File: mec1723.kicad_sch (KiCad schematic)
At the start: 62 parts, among them SW3001 SW_B3U-1000P_SMD, SW3002 SW_B3U-1000P_SMD, SW3003 SW_B3U-1000P_SMD, U3001 MEC1723N-B0-I/SZ, Y3001 Resonator_32.768kHz_ECX-31B

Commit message: [#103224] Add strapping pins, check for signals needed to boot, add breakout connectors, add testpoints
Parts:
- added J3001, J3002, J3003, J3004, J3005, J3006, J3007, J3008, J3009: PinHeader_2x5_P1.27mm_SMD, antmicro-footprints:PinHeader_2x5_P1.27mm_SMD, symbol Antmicro Symbols:PinHeader_2x5_P1.27mm_SMD
- added R3033, R3034, R3035, R3036: R_10k_0402, antmicro-footprints:R_0402_1005Metric, symbol Antmicro Symbols:R_10k_0402
- added TP3008, TP3009, TP3010, TP3011, TP3012: TP_1mm_SMD, antmicro-footprints:TP_SMD_1mm, symbol antmicroTestPoints:TP_1mm_SMD
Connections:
- net +1V8: now also J3004.3, TP3008.1
- net +3V3: now also TP3001.1, J3003.7, J3004.1, R3033.2, R3035.2, TP3009.1, TP3011.1
- net 7SEG_H.A: now also U3001.N10 (GPIO152/KSO14/GPTP_OUT3/I2C07_SDA_ALT)
- net 7SEG_H.B: now also U3001.B9 (GPIO254)
- net 7SEG_H.C: now also U3001.A13 (GPIO156/LED0)
- net 7SEG_H.D: now also U3001.B13 (GPIO157/LED1)
- net 7SEG_H.DP: now also U3001.A9 (GPIO165/32KHZ_IN/CTOUT0)
- net 7SEG_H.E: now also U3001.C12 (GPIO153/LED2)
- net 7SEG_H.F: now also U3001.E13 (GPIO035/PWM8/CTOUT1/ICT15/LED3)
- net 7SEG_H.G: now also U3001.C13 (GPIO175/CMP_VOUT1/PWM8_ALT)
- net 7SEG_H.~{OE1}: now also U3001.C1 (GPIO221/32KHz_OUT/GPTP_IN3/CMP_VIN1/SYS-_SHDN_FW#)
- net 7SEG_H.~{OE2}: now also U3001.B8 (GPIO241/CMP_VOUT0/PWM0_ALT)
- net 7SEG_L.A: now also U3001.L7 (GPIO020/KSI1)
- net 7SEG_L.B: now also U3001.N9 (GPIO021/KSI2)
- net 7SEG_L.C: now also U3001.J9 (GPIO030/KSI5/I2C10_SDA/TIN3)
- net 7SEG_L.D: now also U3001.M11 (GPIO031/KSI6/GPTP_OUT1)
- net 7SEG_L.DP: now also U3001.J5 (GPIO064/SLP_S0#)
- net 7SEG_L.E: now also U3001.M10 (GPIO040/GPTP_OUT2/KSO00)
- net 7SEG_L.F: now also U3001.J12 (GPIO042/PECI_DAT/SB-TSI_DAT)
- net 7SEG_L.G: now also U3001.J13 (GPIO043/SB-TSI_CLK)
- net 7SEG_L.~{OE1}: now also U3001.G13 (GPIO240)
- net 7SEG_L.~{OE2}: now also U3001.L9 (GPIO151/ICT4/KSO15)
- net CMP_STRAP: now also R3033.1, R3034.2
- net DC_SCM_P3V0: now also TP3010.1
- net GND: now also R3032.1, J3003.9, J3004.5, J3004.7, J3004.9, R3034.1, R3036.1, TP3012.1
- net PWRGD_S0iX: now also J3003.5
- net UART_BSTRAP: now also R3035.1, R3036.2
- net GPIO143: now reaches R3013.1, U3001.A7 (GPIO143/I2C04_SDA/UART0_CTS#/SPI1_MISO/UART0_DTR#_ALT)
- net GPIO143: now also J3001.8
- net GPIO154: now reaches R3009.1, U3001.A12 (GPIO154/I2C02_SDA/CPU_C10)
- net GPIO154: now also J3008.10
- net GPIO131: now reaches R3008.1, U3001.N7 (GPIO131/I2C01_SCL/SLV_SPI_CS#/TOUT0)
- net GPIO131: now also J3008.8
- net GPIO004: now reaches R3022.1, U3001.C6 (GPIO004/I2C00_SCL/SPI0_MOSI)
- net GPIO004: now also J3006.6
- net GPIO010: now reaches R3012.1, U3001.C10 (GPIO010/I2C03_SCL/PS2_DAT0B)
- net GPIO010: now also J3001.6
- net GPIO003: now reaches R3021.1, U3001.F5 (GPIO003/I2C00_SDA/SPI0_CS0#)
- net GPIO003: now also J3006.4
- net GPIO242: now reaches U3001.A10 (GPIO242/VCC_PWRGD_ALT)
- net GPIO242: now also J3002.1
- net GPIO224: now reaches U3001.A11 (GPIO244/UART_CLK_ALT/PWROK_ALT)
- net GPIO224: now also J3005.5
- net GPIO062: now reaches U3001.A2 (GPIO062/I2C11_SCL(RESET#))
- net GPIO062: now also J3005.1
- net GPIO246: now reaches U3001.B10 (GPIO246/PWRGD_S0iX_ALT2/CTOUT1_ALT)
- net GPIO246: now also J3005.7
- net GPIO000: now reaches U3001.B3 (SYSPWR_PRES&VCI_IN3#/GPIO000/I2C11_SDA)
- net GPIO106: now reaches U3001.E3 (GPIO106/PWROK/CMP_VREF1)
- net GPIO106: now also J3005.3
- net GPIO067: now reaches U3001.L2 (GPIO067/VREF2_ADC)
- net GPIO067: now also J3004.10
- net GPIO222: now reaches U3001.L5 (GPIO222/PROCHOT_IN#_ALT)
- net GPIO222: now also J3002.3
- net GPIO002: now reaches U3001.M8 (GPIO002/PWM5/SHD_CS1#)
- net GPIO002: now also J3006.3
- net GPIO144: now reaches R3014.1, U3001.E7 (GPIO144/I2C04_SCL/UART0_RTS#/SPI1_CS#/UART0_RI#_ALT)
- net GPIO144: now also J3001.10
- net GPIO012: now reaches R3019.1, U3001.N6 (GPIO012/I2C07_SDA/SLV_SPI_IO2/TOUT3)
- net GPIO012: now also J3002.10
- net GPIO142: now reaches R3016.1, U3001.F7 (GPIO142/I2C05_SCL/SPI1_MOSI/UART0_DSR#_ALT)
- net GPIO142: now also J3002.4
- net GPIO112: now reaches U3001.K13 (GPIO112/KSO05(DSW_PWRGD))
- net GPIO112: now also J3008.3; no longer TP3001.1
- net GPIO130: now reaches R3007.1, U3001.N8 (GPIO130/I2C01_SDA/SLV_SPI_IO0/TOUT1)
- net GPIO130: now also J3008.6
- net BGP01: now reaches U3001.A4 (BGPO1/GPIO101)
- net BGP01: now also J3003.8
- net BGP00: now reaches U3001.A5 (BGPO0)
- net BGP00: now also J3003.6
- net ~{VCI_IN1}: now reaches U3001.A6 (VCI_IN1#/GPIO162)
- net ~{VCI_IN1}: now also J3003.2
- net GPIO051: now reaches U3001.B1 (GPIO051/ICT1_TACH1/GTACH1)
- net GPIO051: now also J3001.1
- net GPIO245: now reaches U3001.B11 (GPIO245/GPSPI_I00)
- net GPIO245: now also J3009.5, J3009.6
- net GPIO033: now reaches U3001.B2 (GPIO033/TACH3/RC_ID0)
- net GPIO033: now also J3001.7
- net BGP02: now reaches U3001.B5 (BGPO2/GPIO102)
- net BGP02: now also J3003.10
- net GPIO124: now reaches U3001.C11 (GPIO124/PVT_CS#/KS011/ICT12/GPTP_OUT6)
- net GPIO124: now also J3007.9
- net GPIO024: now reaches U3001.C2 (GPIO024/GPSPI_CS#/GTPP_IN6/I2C07_SCL_ALT)
- net GPIO024: now also J3009.3, J3009.4
- net GPIO023: now reaches U3001.C3 (GPIO023/GPSPI_CLK/GPTP_IN7)
- net GPIO023: now also J3009.1, J3009.2
- net ~{VCI_IN2}: now reaches U3001.C4 (VCI_IN2#/GPIO161)
- net ~{VCI_IN2}: now also J3003.4
- net VCI_OUT2: now reaches U3001.C5 (VCI_OUT2)
- net VCI_OUT2: now also J3003.3
- net GPIO243: now reaches U3001.C8 (GPIO243/GPSPI_I01)
- net GPIO243: now also J3009.7, J3009.8
- net GPIO125: now reaches U3001.D11 (GPIO125/PVT_CLK/KS012/GPTP_OUT5)
- net GPIO125: now also J3008.1
- net GPIO122: now reaches U3001.E11 (GPIO122/PVT_I01/KS009)
- net GPIO122: now also J3007.5
- net GPIO123: now reaches U3001.E12 (GPIO123/PVT_I02/KS010)
- net GPIO123: now also J3007.7
- net GPIO022: now reaches U3001.E2 (GPIO022/GPSPI_IO3/GPTP_IN4/32kHz_OUT_ALT)
- net GPIO022: now also J3009.10, J3009.9
- net GPIO046: now reaches U3001.E9 (GPIO046/KS002/ICT11/BCM1_DAT)
- net GPIO046: now also J3007.1
- net VCI_OVRD_IN: now reaches U3001.F1 (VCI_OVRD_IN)
- net VCI_OVRD_IN: now also J3003.1
- net GPIO121: now reaches U3001.F12 (GPIO121/PVT_I00/KS008)
- net GPIO121: now also J3007.3
- net GPIO047: now reaches U3001.F13 (GPIO047/KS003/PWM3_ALT/ICT13/BCM1_CLK)
- net GPIO047: now also J3005.9
- net GPIO050: now reaches U3001.F3 (GPIO050/ICT0_TACH0/GTACH0)
- net GPIO050: now also J3001.3
- net GPIO204: now reaches U3001.H2 (GPIO204/ADC04)
- net GPIO204: now also J3004.4
- net GPIO200: now reaches U3001.H3 (GPIO200/ADC00/TRACEDATA0)
- net GPIO200: now also J3006.5
- net GPIO114: now reaches U3001.H9 (GPIO114/PS2_CLK0A/nEC_SCI)
- net GPIO114: now also U3001.N12 (GPIO115/PS2_DAT0A), J3008.7, J3008.9
- net GPIO203: now reaches U3001.J1 (GPIO203/ADC03/TRACEDATA3)
- net GPIO203: now also J3004.2
- net GPIO113: now reaches U3001.J11 (GPIO113/KSO06/ICT9)
- net GPIO113: now also J3008.5
- net GPIO202: now reaches U3001.J2 (GPIO202/ADC02/TRACEDATA2)
- net GPIO202: now also J3006.9
- net GPIO201: now reaches U3001.J3 (GPIO201/ADC01/TRACEDATA1)
- net GPIO201: now also J3006.7
- net GPIO015: now reaches U3001.J7 (GPIO015/PWM7/ICT10)
- net GPIO015: now also J3002.9
- net GPIO205: now reaches U3001.K3 (GPIO205/ADC05)
- net GPIO205: now also J3004.6
- net GPIO206: now reaches U3001.L1 (GPIO206/ADC06)
- net GPIO206: now also J3004.8
- net GPIO054: now reaches U3001.L12 (GPIO054/PWM1/SLV_SPI_SCLK/GPWM1)
- net GPIO054: now also J3002.5
- net GPIO052: now reaches U3001.L8 (GPIO052/ICT2_TACH2)
- net GPIO052: now also J3001.5
- net GPIO053: now reaches U3001.M13 (GPIO053/PWM0/SLV_SPI_MSTR_INT/GPWM0)
- net GPIO053: now also J3001.9
- net GPIO014: now reaches U3001.M9 (GPIO014/PWM6/SLV_SPI_IO1/GPTP_IN2)
- net GPIO014: now also J3002.7
- net GPIO155: now reaches R3010.1, U3001.C9 (GPIO155/I2C02_SCL(SYSPWR_VALID))
- net GPIO155: now also J3001.2
- net GPIO007: now reaches R3011.1, U3001.B12 (GPIO007/I2C03_SDA/PS2_CLK0B)
- net GPIO007: now also J3001.4
- net GPIO013: now reaches R3020.1, U3001.M7 (GPIO013/I2C07_SCL/SLV_SPI_IO3/TOUT2)
- net GPIO013: now also J3006.1
- net GPIO141: now reaches R3015.1, U3001.B7 (GPIO141/I2C05_SDA/SPI1_CLK/UART0_DCD#_ALT)
- net GPIO141: now also J3002.2
- net GPIO255: now reaches U3001.B6 (GPIO255/UART1_RX_ALT/UART1_DSR#)
- net GPIO255: now also J3007.8
- net GPIO060: now reaches U3001.D2 (GPIO060/KBRST/TST_-CLK_OUT/UART1_DCD#/SPI0_CS1#)
- net GPIO060: now also J3007.4
- net GPIO171: now reaches U3001.G9 (GPIO171/UART1_RX/TFDP_DATA)
- net GPIO171: now also J3005.2
- net GPIO034: now reaches R3024.1, U3001.H12 (GPIO034/GPSPI_IO2/RC_ID1/SPI0_CLK)
- net GPIO034: now also J3006.10
- net GPIO036: now reaches R3023.1, U3001.H13 (GPIO036/RC_ID2/SPI0_MISO)
- net GPIO036: now also J3006.8
- net GPIO100: now reaches U3001.H7 (GPIO100/nEC_SCI_ALT/ICT6)
- net GPIO100: now also J3006.2
- net GPIO011: now reaches U3001.J6 (GPIO011/nSMI_ALT/PWM4/ICT7)
- net GPIO011: now also J3008.2
- net GPIO120: now reaches U3001.K12 (GPIO120/KSO07/UART1_DTR#)
- net GPIO120: now also J3007.6
- net GPIO140: now reaches R3018.1, U3001.L11 (GPIO140/I2C06_SCL/ICT5/KSO17)
- net GPIO140: now also J3002.8
- net GPIO107: now reaches U3001.L13 (GPIO107/nSMI/KSO04/I2C10_SCL)
- net GPIO107: now also J3008.4
- net GPIO025: now reaches U3001.M12 (GPIO025/nEMI_INT/UART_CLK/UART1_RI#/TIN0)
- net GPIO025: now also J3007.10
- net GPIO132: now reaches R3017.1, U3001.N11 (GPIO132/I2C06_SDA/KSO16)
- net GPIO132: now also J3002.6
- net ~{UART0_CTS} renamed GPIO127
- net GPIO127: now also J3005.4
- net ~{UART0_DCD} renamed GPIO17
- net GPIO17: now also J3005.6
- net ~{UART0_DSR} renamed GPIO027
- net GPIO027: now also J3005.10
- net ~{UART0_DTR} renamed GPIO026
- net GPIO026: now also J3005.8
- net ~{UART0_RI} renamed GPIO032
- net GPIO032: now also J3007.2
- no-connect marks 2 -> 0
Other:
- note added: "Boot Source Select Strap: - 1(R5010 not mounted)=Use the shared SPI pins for boot - 0(R5010 mounted)=Use the eSPI Flash Channel for boot"
- note added: "Check if needed"
- note added: "PIN BREAKOUT"
- note added: "PVT Flash"
- note removed: "ADC pins"
- note removed: "Boot Source Select Strap: 1(R5010 not mounted)=Use the shared SPI pins for boot 0(R5010 mounted)=Use the eSPI Flash Channel for boot"
- note removed: "Connect GPIO after connecting all other, most important signals"
- note removed: "Private QSPI Flash"
- moved on the sheet: C3007, C3008, C3009, C3010, C3013, C3015, C3016, C3018, R3001, R3002, R3005, R3006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

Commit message: [#103224] Add pullup resistors to VCI_IN#, add pulldown to nRSMRST, add schottky diode on VBAT
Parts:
- removed C3001: C_1u_6.3V_X6S_0402, antmicro-footprints:C_0402_1005Metric, symbol Antmicro Symbols:C_1u_6.3V_X6S_0402
- removed C3014, C3015, C3016, C3017: C_1u_10V_X7R_0603, antmicro-footprints:C_0603_1608Metric, symbol Antmicro Symbols:C_1u_10V_X7R_0603
- added C3001, C3014, C3015, C3016, C3017: C_1u_0603, antmicro-footprints:C_0603_1608Metric, symbol Antmicro Symbols:C_1u_0603
- added D3001: BAT54-02V-G3-08, antmicro-footprints:SOD-523, symbol Antmicro Symbols:BAT54-02V-G3-08
- added R3037: R_1k_0402, antmicro-footprints:R_0402_1005Metric, symbol Antmicro Symbols:R_1k_0402
- added R3038, R3039, R3040: R_100k_0402, antmicro-footprints:R_0402_1005Metric, symbol Antmicro Symbols:R_100k_0402
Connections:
- net +1V8: now also C3016.2
- net +3V3: now also C3015.2, C3017.2
- net GND: now also C3001.1, C3014.1, C3015.1, C3016.1, C3017.1, R3040.1
- net GPIO171: no longer U3001.G9 (GPIO171/UART1_RX/TFDP_DATA)
- net ~{VCI_IN1}: no longer U3001.A6 (VCI_IN1#/GPIO162)
- net ~{VCI_IN2}: no longer U3001.C4 (VCI_IN2#/GPIO161)
- net at U3001.H1 (VR_CAP): now also C3001.2
- net DC_SCM_P3V0 renamed +3V0
- net +3V0: now also C3014.2, R3037.1, R3038.2, R3039.2; no longer U3001.E5 (VBAT)
- new net: D3001.2 (A), R3037.2
- new net: D3001.1 (C), U3001.E5 (VBAT)
- new net: R3039.1, U3001.C4 (VCI_IN2#/GPIO161)
- new net: R3038.1, U3001.A6 (VCI_IN1#/GPIO162)
- new net ~{RSMRST}: R3040.2, U3001.G9 (GPIO171/UART1_RX/TFDP_DATA)
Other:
- note added: "If the Shared SPI port is used for booting, then any unused GPIO may be used for RSMRST#."
- note added: "SPI Flash used - ~{RSMRST} signal can be on any GPIO"
- note removed: "Alt fundtion: RSMRST#"
- note removed: "VTR1: VTR2: - eSPI"
- moved on the sheet: C3002, C3003, C3004, C3005, C3006, C3007, C3008, C3009, C3010, C3011, C3012, C3013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

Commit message: [#103224] Add UART1, added GND to breakout connectors, fix orientation of DC-SCM connector, delete unused notes
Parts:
- added J3010, J3011: PinHeader_2x5_P1.27mm_SMD, antmicro-footprints:PinHeader_2x5_P1.27mm_SMD, symbol Antmicro Symbols:PinHeader_2x5_P1.27mm_SMD
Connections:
- net 7SEG_H.~{OE2} is gone; now on net 7SEG_H.DP: U3001.B8 (GPIO241/CMP_VOUT0/PWM0_ALT)
- net 7SEG_L.~{OE1} is gone; now on net 7SEG_L.F: U3001.G13 (GPIO240)
- net 7SEG_L.~{OE2} is gone; now on net 7SEG_L.DP: U3001.L9 (GPIO151/ICT4/KSO15)
- net +1V8: no longer J3004.3
- net +3V3: no longer J3003.7, J3004.1
- net 7SEG_H.DP: no longer U3001.A9 (GPIO165/32KHZ_IN/CTOUT0)
- net 7SEG_L.DP: no longer U3001.J5 (GPIO064/SLP_S0#)
- net 7SEG_L.F: no longer U3001.J12 (GPIO042/PECI_DAT/SB-TSI_DAT)
- net BGP00: now also J3004.1; no longer J3003.6
- net GND: now also J3001.5, J3001.6, J3002.5, J3002.6, J3003.5, J3003.6, J3004.6, J3005.5, J3005.6, J3006.5, J3006.6, J3007.5, J3007.6, J3008.5, J3008.6, J3009.5, J3009.6, J3010.5, J3010.6, J3011.6; no longer J3003.9, J3004.7, J3004.9
- net GPIO004: now also J3010.8; no longer J3006.6
- net GPIO010: now also J3010.7; no longer J3001.6
- net GPIO052: now also J3011.2; no longer J3001.5
- net GPIO054: now also J3011.3; no longer J3002.5
- net GPIO113: now also J3011.1; no longer J3008.5
- net GPIO120: now also J3010.9; no longer J3007.6
- net GPIO122: now also J3011.8; no longer J3007.5
- net GPIO130: now also J3010.1; no longer J3008.6
- net GPIO132: now also J3011.10; no longer J3002.6
- net GPIO17: now also J3010.3; no longer J3005.6
- net GPIO200: now also J3010.10; no longer J3006.5
- net GPIO205: now also J3011.4; no longer J3004.6
- net GPIO224: now also J3010.4; no longer J3005.5
- net GPIO245: now also J3010.2; no longer J3009.5, J3009.6
- net GPIO255: no longer U3001.B6 (GPIO255/UART1_RX_ALT/UART1_DSR#)
- net PWRGD_S0iX: now also J3004.3; no longer J3003.5
- net ~{RSMRST}: now also U3001.B6 (GPIO255/UART1_RX_ALT/UART1_DSR#); no longer U3001.G9 (GPIO171/UART1_RX/TFDP_DATA)
- net 7SEG_H.~{OE1} renamed 32kHz_OUT
- net 32kHz_OUT: now also J3003.9
- net EC_UART.RX renamed EC_UART0.RX
- net EC_UART.TX renamed EC_UART0.TX
- net JTAG_STRAP: no longer names the net of R3029.2, R3030.1
- net JTAG_STRAP: no longer U3001.G12 (GPIO170/UART1_TX/TFDP_CLK[JTAG_STRAP])
- new net 32kHz_IN: J3003.7, U3001.A9 (GPIO165/32KHZ_IN/CTOUT0)
- new net EC_UART1.RX: U3001.G9 (GPIO171/UART1_RX/TFDP_DATA)
- new net EC_UART1.TX: U3001.G12 (GPIO170/UART1_TX/TFDP_CLK[JTAG_STRAP])
- new net PECI_DAT: J3004.9, U3001.J12 (GPIO042/PECI_DAT/SB-TSI_DAT)
- new net SLP_S0#: J3004.7, U3001.J5 (GPIO064/SLP_S0#)
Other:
- note added: "JTAG_STRAP"
- note removed: "If the Shared SPI port is used for booting, then any unused GPIO may be used for RSMRST#."
- moved on the sheet: R3029

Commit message: [#103224] Add notes to schematic, fix typos, fix gpio connections, bump date
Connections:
- net ~{VCI_IN1} is gone; now on net GPIO000: J3003.2
- net ~{VCI_IN2} is gone; now on net GPIO054: J3003.4
- net GPIO054: no longer J3011.3
- net GPIO114: no longer J3008.9, U3001.N12 (GPIO115/PS2_DAT0A)
- new net GPIO115: J3008.9, U3001.N12 (GPIO115/PS2_DAT0A)
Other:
- note removed: "Check if needed"
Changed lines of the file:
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@@
 		)
 	)
-	(text "Check if needed"
-		(exclude_from_sim no)
-		(at 272.542 30.988 0)
-		(effects
-			(font
-				(size 1.27 1.27)
-			)
-		)
-	)
 	(text "Boot Source Select Strap:\n- 1(R5010 not mounted)=Use the shared \nSPI pins for boot\n\n- 0(R5010 mounted)=Use the eSPI \nFlash Channel for boot"
 		(exclude_from_sim no)
@@
 	(wire
 		(pts
-			(xy 354.33 40.64) (xy 364.49 40.64)
-		)
-		(stroke
-			(width 0)
-			(type default)
-		)
-	)
-	(wire
-		(pts
 			(xy 347.98 64.77) (xy 347.98 67.31)
 		)
@@
 		)
 	)
-	(label "GPIO114"
+	(label "GPIO115"
 		(at 354.33 173.99 0)
 		(effects
@@
 		)
 	)
+	(label "GPIO054"
+		(at 374.65 228.6 0)
+		(effects
+			(font
+				(size 1.27 1.27)
+			)
+			(justify left bottom)
+		)
+	)
 	(label "EC_QSPI.SCK"
 		(at 294.64 62.23 0)
@@
 		)
 	)
-	(label "~{VCI_IN2}"
-		(at 374.65 228.6 0)
-		(effects
-			(font
-				(size 1.27 1.27)
-			)
-			(justify left bottom)
-		)
-	)
 	(label "EC_QSPI.IO3"
 		(at 294.64 54.61 0)
@@
 		)
 	)
-	(label "GPIO114"
+	(label "GPIO115"
 		(at 261.62 191.77 0)
 		(effects
@@
 		)
 	)
-	(label "GPIO054"
-		(at 354.33 40.64 0)
-		(effects
-			(font
-				(size 1.27 1.27)
-			)
-			(justify left bottom)
-		)
-	)
 	(label "GPIO013"
 		(at 354.33 123.19 0)
@@
 		)
 	)
-	(label "~{VCI_IN1}"
-		(at 374.65 226.06 0)
-		(effects
-			(font
-				(size 1.27 1.27)
-			)
-			(justify left bottom)
-		)
-	)
 	(label "GPIO131"
 		(at 374.65 171.45 0)
@@
 		(effects
 			(font
+				(size 1.27 1.27)
+			)
+			(justify left bottom)
+		)
+	)
+	(label "GPIO000"
+		(at 374.65 226.06 0)
+		(effects
+			(font

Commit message: chore: set date and project name
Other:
- company: (none) -> Antmicro
- title: (none) -> eSPI Adapter
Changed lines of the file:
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@@
 	(generator_version "10.0")
 	(paper "A3")
+	(title_block
+		(title "eSPI Adapter")
+		(date "2026-08-21")
+		(rev "1.0.0")
+		(company "Antmicro")
+	)
 	(rectangle
 		(start 115.57 139.7)

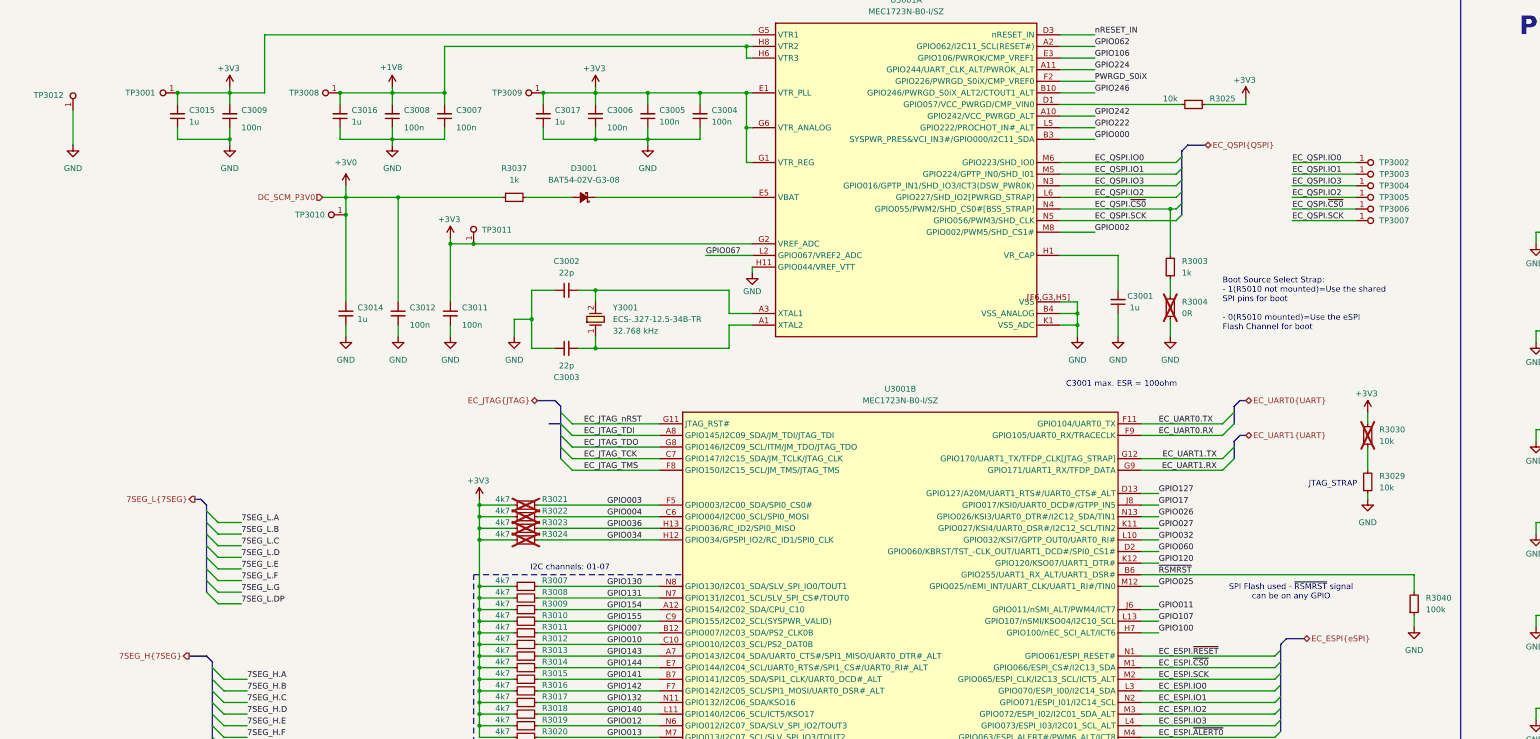
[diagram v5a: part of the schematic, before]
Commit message: [#103696] Initial placement of all components, delete redundant testpoints
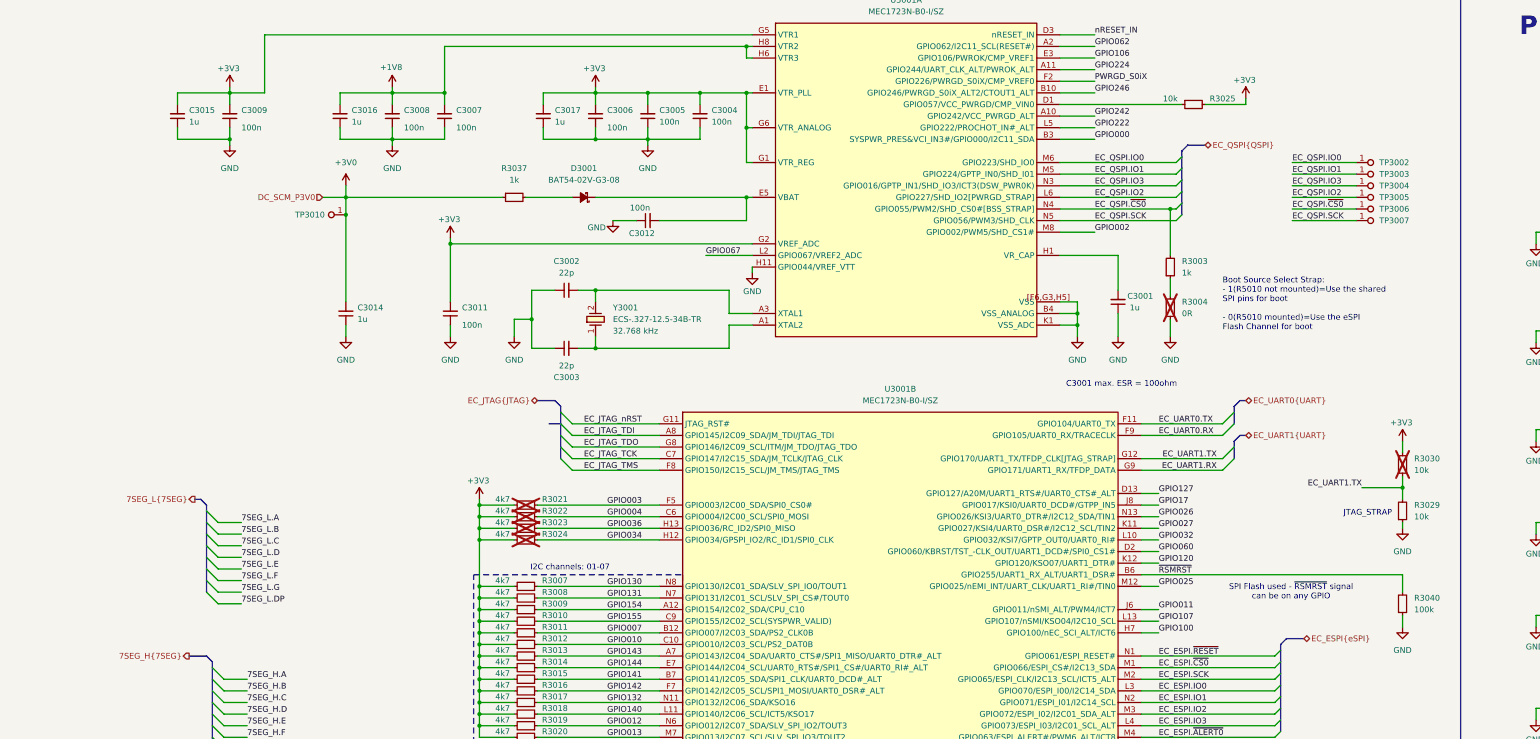
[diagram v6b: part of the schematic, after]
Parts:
- removed TP3001, TP3008, TP3009, TP3011, TP3012: TP_1mm_SMD, antmicro-footprints:TP_SMD_1mm, symbol antmicroTestPoints:TP_1mm_SMD
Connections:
- net +3V0: no longer C3012.2
- net EC_UART1.TX: now also R3029.2, R3030.1
- net at D3001.1 (C), U3001.E5 (VBAT): now also C3012.2
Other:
- moved on the sheet: R3029, R3030, R3040
